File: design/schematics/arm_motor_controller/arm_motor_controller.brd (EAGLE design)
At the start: 71.8 x 54.6 mm, 60 parts, among them Q1 PFET-FQP27P06, Q2 PFET-FQP27P06, Q3 NFET-FQP30N06L, Q4 NFET-FQP30N06L, Q5 PFET-FQP27P06, Q6 PFET-FQP27P06, Q7 NFET-FQP30N06L, Q8 NFET-FQP30N06L, U1 V_REG_LD1085D2

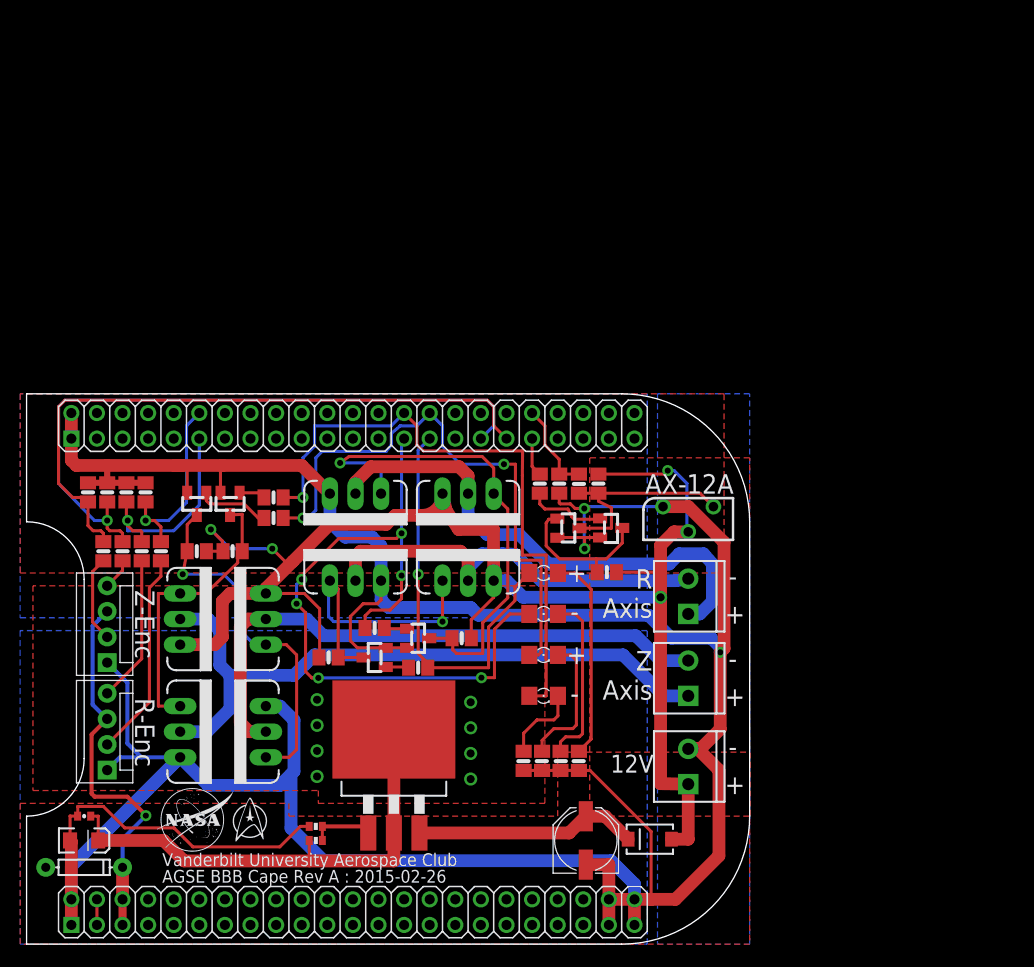
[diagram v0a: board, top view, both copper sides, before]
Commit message: updated adafruit library
to have a version of the board which only shows the outline, but doesn't
set the dimension layer.  also added the adafruit library to the repo
for use with other schematics.
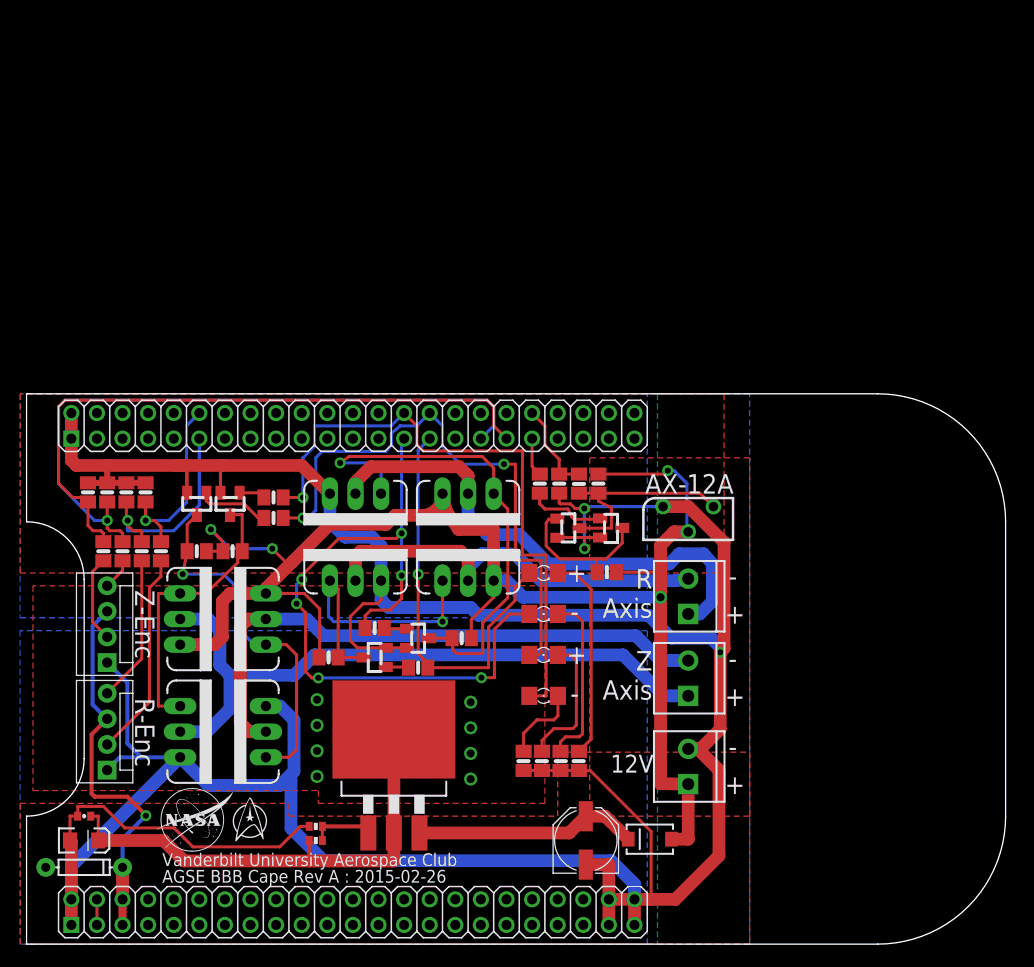
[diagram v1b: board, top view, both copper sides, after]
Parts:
- U$1: value BEAGLEBONE_OUTLINE -> BEAGLEBONE_OUTLINENO_DIM
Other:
- board size 71.8 x 54.6 mm -> 97.2 x 54.6 mm
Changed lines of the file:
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@@
 <layer number="14" name="Route14" color="1" fill="6" visible="no" active="no"/>
 <layer number="15" name="Route15" color="4" fill="6" visible="no" active="no"/>
-<layer number="16" name="Bottom" color="1" fill="1" visible="yes" active="yes"/>
+<layer number="16" name="Bottom" color="1" fill="1" visible="no" active="yes"/>
 <layer number="17" name="Pads" color="2" fill="1" visible="yes" active="yes"/>
 <layer number="18" name="Vias" color="2" fill="1" visible="yes" active="yes"/>
@@
 <layer number="20" name="Dimension" color="15" fill="1" visible="yes" active="yes"/>
 <layer number="21" name="tPlace" color="7" fill="1" visible="yes" active="yes"/>
-<layer number="22" name="bPlace" color="7" fill="1" visible="yes" active="yes"/>
+<layer number="22" name="bPlace" color="7" fill="1" visible="no" active="yes"/>
 <layer number="23" name="tOrigins" color="15" fill="1" visible="yes" active="yes"/>
-<layer number="24" name="bOrigins" color="15" fill="1" visible="yes" active="yes"/>
+<layer number="24" name="bOrigins" color="15" fill="1" visible="no" active="yes"/>
 <layer number="25" name="tNames" color="7" fill="1" visible="yes" active="yes"/>
-<layer number="26" name="bNames" color="7" fill="1" visible="yes" active="yes"/>
+<layer number="26" name="bNames" color="7" fill="1" visible="no" active="yes"/>
 <layer number="27" name="tValues" color="7" fill="1" visible="yes" active="yes"/>
-<layer number="28" name="bValues" color="7" fill="1" visible="yes" active="yes"/>
+<layer number="28" name="bValues" color="7" fill="1" visible="no" active="yes"/>
 <layer number="29" name="tStop" color="7" fill="3" visible="no" active="yes"/>
 <layer number="30" name="bStop" color="7" fill="6" visible="no" active="yes"/>
@@
 <layer number="56" name="wert" color="7" fill="1" visible="no" active="no"/>
 <layer number="57" name="tCAD" color="7" fill="1" visible="no" active="no"/>
+<layer number="59" name="tCarbon" color="7" fill="1" visible="no" active="no"/>
+<layer number="60" name="bCarbon" color="7" fill="1" visible="no" active="no"/>
 <layer number="90" name="Modules" color="5" fill="1" visible="no" active="no"/>
 <layer number="91" name="Nets" color="2" fill="1" visible="no" active="no"/>
@@
 <layer number="113" name="IDFDebug" color="4" fill="1" visible="no" active="yes"/>
 <layer number="116" name="Patch_BOT" color="9" fill="4" visible="no" active="yes"/>
+<layer number="118" name="Rect_Pads" color="7" fill="1" visible="no" active="no"/>
 <layer number="121" name="_tsilk" color="7" fill="1" visible="no" active="yes"/>
 <layer number="122" name="_bsilk" color="7" fill="1" visible="no" active="yes"/>
@@
 <layer number="127" name="_tValues" color="7" fill="1" visible="no" active="yes"/>
 <layer number="128" name="_bValues" color="7" fill="1" visible="no" active="yes"/>
+<layer number="129" name="Mask" color="7" fill="1" visible="no" active="yes"/>
 <layer number="131" name="tAdjust" color="7" fill="1" visible="no" active="yes"/>
 <layer number="132" name="bAdjust" color="7" fill="1" visible="no" active="yes"/>
@@
 <layer number="155" name="FabDoc3" color="7" fill="15" visible="no" active="no"/>
 <layer number="199" name="Contour" color="7" fill="1" visible="no" active="yes"/>
-<layer number="200" name="200bmp" color="1" fill="10" visible="yes" active="yes"/>
+<layer number="200" name="200bmp" color="1" fill="10" visible="no" active="yes"/>
 <layer number="201" name="201bmp" color="2" fill="10" visible="no" active="yes"/>
 <layer number="202" name="202bmp" color="3" fill="1" visible="no" active="no"/>
@@
 <layer number="230" name="230bmp" color="7" fill="1" visible="no" active="yes"/>
 <layer number="231" name="231bmp" color="7" fill="1" visible="no" active="yes"/>
+<layer number="232" name="Eagle3D_PG2" color="7" fill="1" visible="no" active="no"/>
+<layer number="233" name="Eagle3D_PG3" color="7" fill="1" visible="no" active="no"/>
 <layer number="248" name="Housing" color="7" fill="1" visible="no" active="yes"/>
 <layer number="249" name="Edge" color="7" fill="1" visible="no" active="yes"/>
@@
 <rectangle x1="61.7601" y1="38.2905" x2="61.9125" y2="38.3667" layer="22" rot="R180"/>
 <rectangle x1="55.0545" y1="38.2905" x2="55.3593" y2="38.3667" layer="22" rot="R180"/>
+<wire x1="88.519" y1="0.254" x2="4.064" y2="0.254" width="0.127" layer="20"/>
+<wire x1="101.219" y1="42.164" x2="88.519" y2="54.864" width="0.127" layer="20" curve="90"/>
+<wire x1="88.519" y1="0.254" x2="101.219" y2="12.954" width="0.127" layer="20" curve="90"/>
+<wire x1="101.219" y1="42.164" x2="101.219" y2="12.954" width="0.127" layer="20"/>
+<wire x1="88.519" y1="54.864" x2="4.064" y2="54.864" width="0.127" layer="20"/>
+<wire x1="4.064" y1="54.864" x2="4.064" y2="42.164" width="0.127" layer="20"/>
+<wire x1="4.064" y1="12.954" x2="4.064" y2="0.254" width="0.127" layer="20"/>
+<wire x1="9.779" y1="36.449" x2="9.779" y2="18.669" width="0.127" layer="20"/>
+<wire x1="9.779" y1="36.449" x2="4.064" y2="42.164" width="0.127" layer="20" curve="90"/>
+<wire x1="9.779" y1="18.669" x2="4.064" y2="12.954" width="0.127" layer="20" curve="-90"/>
 </plain>
 <attributes>
@@
 </autorouter>
 <elements>
-<element name="U$1" library="adafruit" package="BEAGLEBONE_SHIELD" value="BEAGLEBONE_OUTLINE" x="-10.541" y="54.864" smashed="yes" rot="R270"/>
+<element name="U$1" library="adafruit" package="BEAGLEBONE_SHIELD" value="BEAGLEBONE_OUTLINENO_DIM" x="-10.541" y="54.864" smashed="yes" rot="R270"/>
 <element name="U1" library="SparkFun-PowerIC" package="D2PACK/A" value="V_REG_LD1085D2" x="40.513" y="19.558" smashed="yes">
 <attribute name="MANEX" value="140-0004281" x="40.513" y="19.558" size="1.778" layer="27" display="off"/>
@@
 <signals>
 <signal name="VDD_3V3EXP">
+<wire x1="11.049" y1="4.699" x2="11.049" y2="2.159" width="0.3048" layer="1"/>
 <contactref element="U$1" pad="49"/>
 <contactref element="U$1" pad="50"/>
-<wire x1="11.049" y1="4.699" x2="11.049" y2="2.159" width="0.3048" layer="1"/>
 </signal>
 <signal name="AIN0">

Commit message: working on schematic/board.
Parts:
- removed R1: 370, SparkFun-Passives:0402-RES
- removed R2: 1.5k, SparkFun-Passives:0402-RES
- removed U1: V_REG_LD1085D2, SparkFun-PowerIC:D2PACK/A
- added +HLS, +RLS, -HLS, -RLS: M02POLAR, SparkFun-Connectors:MOLEX-1X2
- added D7: (no value), SparkFun-LED:FKIT-LED-1206
- added LD1085: V_REG_317SINK, SparkFun-PowerIC:TO220-ADJ
- added R28: 50, resistor:M0805
- added SERVO1: AX-12A, molex-spox:SPOX-3
- moved Q7 45.2 mm to (64.5, 20.8), turned to 0 degrees
- moved Q8 37.6 mm to (64.5, 29.3), turned to 180 degrees
- moved Q5 36.0 mm to (53.3, 20.8), turned to 0 degrees
- moved Q3 29.6 mm to (64.4, 34.5), turned to 0 degrees
- moved Q4 28.5 mm to (64.4, 43.2), turned to 180 degrees
- moved R4 26.6 mm to (39.2, 17.1)
- moved R5 26.3 mm to (35.2, 17.1)
- moved Q6 25.7 mm to (53.3, 29.3), turned to 180 degrees
- moved JP1 25.4 mm to (95.1, 16.1)
- moved R-AXIS 25.4 mm to (95.1, 33.0)
- moved SERVO 25.4 mm to (95.1, 42.4)
- moved Z-AXIS 25.4 mm to (95.1, 24.9)
- moved D1 25.3 mm to (91.2, 10.7)
- moved T6 24.8 mm to (80.5, 51.6)
- moved R26 24.4 mm to (83.3, 18.0)
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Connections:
- removed net N$16: R11.2, T4.B
- removed net N$4: R1.1, R2.2, U1.1
- new net +HEIGHT_LS: +HLS.2, R7.2, T2.B, U$1.44
- new net +RADIUS_LS: +RLS.2, R11.2, T4.B, U$1.43
- new net -HEIGHT_LS: -HLS.2, R6.1, T1.B, U$1.42
- new net -RADIUS_LS: -RLS.2, R10.1, T3.B, U$1.41
- new net N$19: U$1.46
- net 12V: now also SERVO1.P$2
- net BBB_TX: now also D7.A
- net GND: now also +HLS.1, +RLS.1, -HLS.1, -RLS.1, LD1085.ADJ, R28.1, SERVO1.P$3; no longer R2.1
- net N$10: now also U$1.45; no longer R7.2, T2.B
- net N$15: now also U$1.14; no longer R10.1, T3.B
- net N$3: now also LD1085.IN; no longer U1.3
- net N$9: now also D7.C, R28.2; no longer R6.1, T1.B
- net SERVO_TX/RX: now also SERVO1.P$1
- net VOUT: now also LD1085.OUT; no longer R1.2, U1.2, U1.TAB
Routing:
- net GND: track 358.6 -> 0.00 mm, vias 3 -> 0
- net 12V: track 151.3 -> 2.03 mm, vias 4 -> 0
- net -RADIUS: track 71.2 -> 0.00 mm, vias 6 -> 0
- net Z+: track 66.6 -> 0.00 mm
- net -HEIGHT: track 61.7 -> 0.00 mm, vias 1 -> 0
- net BBB_EQEP1B: track 66.6 -> 4.87 mm, vias 1 -> 0
- net BBB_EQEP1A: track 63.9 -> 4.87 mm
- net Z-: track 58.9 -> 0.00 mm
- net +HEIGHT: track 56.9 -> 0.00 mm, vias 2 -> 0
- net R+: track 51.0 -> 0.00 mm
- net N$13: track 49.1 -> 0.00 mm, vias 1 -> 0
- net VOUT: track 48.4 -> 0.00 mm, vias 8 -> 0
- net BBB_TX: track 3.84 -> 45.3 mm, vias 0 -> 2
- net R-: track 41.1 -> 0.00 mm
- net +RADIUS: track 40.7 -> 0.00 mm, vias 1 -> 0
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- removed copper zone on layer 16, net 12V
- removed copper zone on layer 1, net GND
- removed copper zone on layer 16, net GND
- removed copper zone on layer 1, net VOUT
- removed copper zone on layer 16, net VOUT

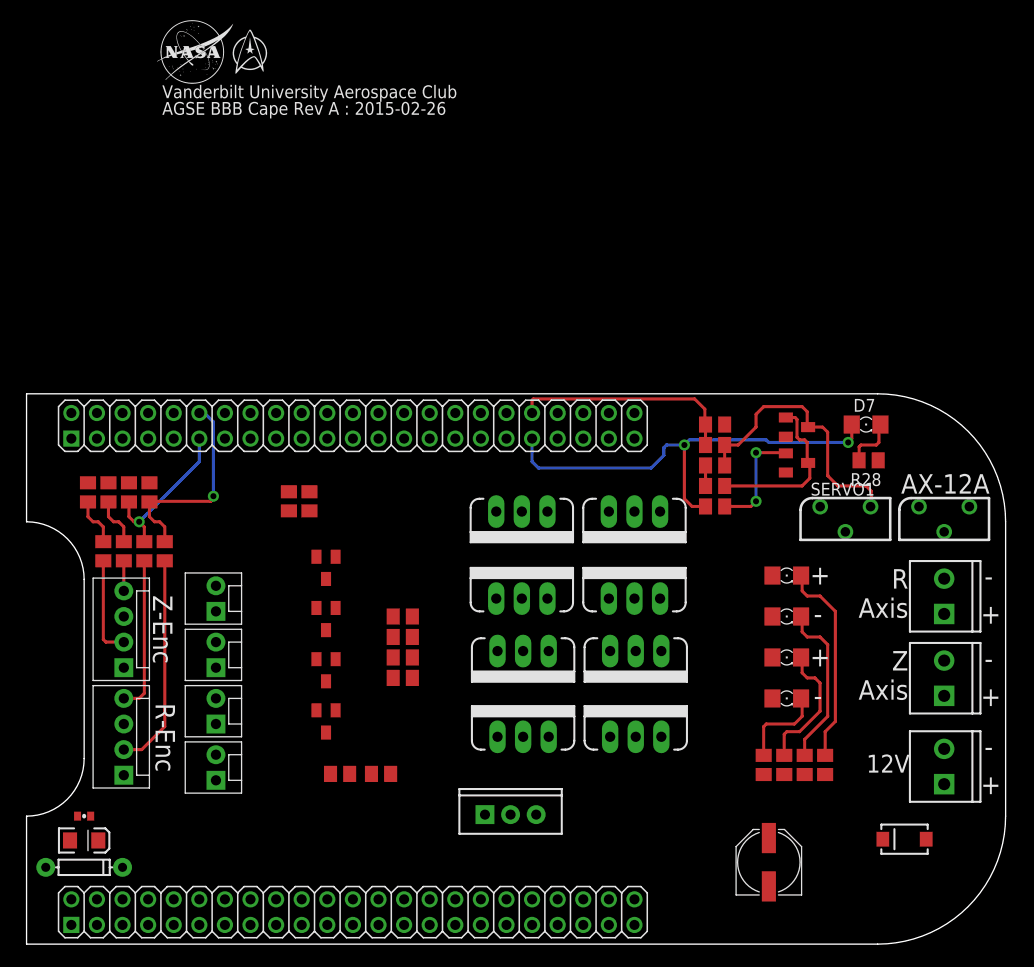
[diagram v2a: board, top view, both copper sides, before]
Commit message: routed the board.
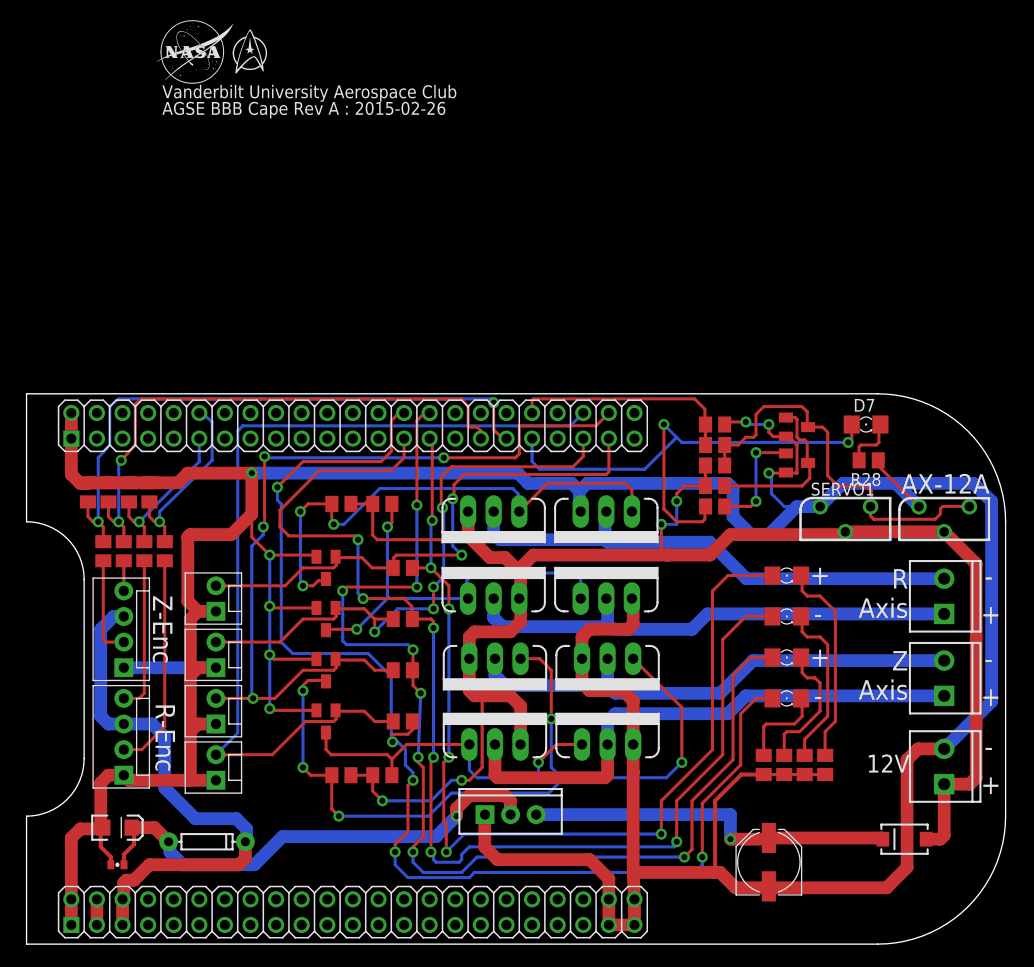
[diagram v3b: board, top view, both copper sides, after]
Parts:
- moved R10 16.3 mm to (41.4, 32.5), turned to 0 degrees
- moved R8 13.4 mm to (39.4, 43.9), turned to 180 degrees
- moved R9 12.7 mm to (35.3, 43.9), turned to 0 degrees
- moved D2 12.5 mm to (22.0, 10.4)
- moved R11 11.4 mm to (41.4, 37.6), turned to 180 degrees
- moved R6 6.35 mm to (41.4, 22.4)
- moved C3 5.85 mm to (13.1, 8.13)
- moved C2 3.54 mm to (13.1, 11.8)
- moved Q5 2.90 mm to (50.5, 20.1)
- moved Q6 2.90 mm to (50.5, 28.6)
- moved Q7 2.90 mm to (61.7, 20.1)
- moved Q8 2.90 mm to (61.7, 28.6)
- moved Q1 2.79 mm to (50.4, 34.5)
- moved Q2 2.79 mm to (50.4, 43.2)
- moved Q3 2.79 mm to (61.6, 34.5)
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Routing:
- net GND: track 0.00 -> 416.1 mm, vias 0 -> 8
- net 12V: track 2.03 -> 166.5 mm, vias 0 -> 4
- net -HEIGHT: track 0.00 -> 121.5 mm, vias 0 -> 5
- net -RADIUS: track 0.00 -> 118.1 mm, vias 0 -> 6
- net +HEIGHT: track 0.00 -> 112.7 mm, vias 0 -> 8
- net +RADIUS: track 0.00 -> 99.0 mm, vias 0 -> 6
- net -HEIGHT_LS: track 0.00 -> 88.5 mm
- net +HEIGHT_LS: track 0.00 -> 82.5 mm, vias 0 -> 4
- net N$8: track 0.00 -> 81.6 mm, vias 0 -> 5
- net -RADIUS_LS: track 0.00 -> 58.4 mm, vias 0 -> 4
- net BBB_EQEP1A: track 4.87 -> 59.7 mm, vias 0 -> 2
- net +RADIUS_LS: track 0.00 -> 54.3 mm, vias 0 -> 2
- net Z+: track 0.00 -> 54.2 mm
- net 5V: track 0.00 -> 53.8 mm
- net N$14: track 0.00 -> 52.3 mm, vias 0 -> 3
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
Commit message: working on updating the board routing.
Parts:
- moved R8 18.3 mm to (39.6, 25.7), turned to 0 degrees
- moved R9 14.9 mm to (39.6, 29.7)
- moved T4 7.77 mm to (32.3, 30.0), turned to 270 degrees
- moved T3 6.78 mm to (32.3, 25.9), turned to 270 degrees
- moved R5 6.29 mm to (39.6, 21.6)
- moved R11 6.11 mm to (39.6, 31.8)
- moved T2 5.79 mm to (32.3, 21.8), turned to 270 degrees
- moved R10 5.14 mm to (39.6, 27.7)
- moved T1 4.82 mm to (32.3, 17.8), turned to 270 degrees
- moved R7 4.20 mm to (39.6, 23.6)
- moved R6 3.31 mm to (39.6, 19.6)
- moved R4 0.57 mm to (39.6, 17.5), turned to 0 degrees
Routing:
- net -RADIUS: track 118.1 -> 32.9 mm, vias 6 -> 4
- net -HEIGHT: track 121.5 -> 43.4 mm, vias 5 -> 2
- net +HEIGHT: track 112.7 -> 39.1 mm, vias 8 -> 2
- net +RADIUS: track 99.0 -> 26.4 mm, vias 6 -> 2
- net GND: track 416.1 -> 372.8 mm, vias 8 -> 3
- net N$13: track 40.7 -> 65.3 mm, vias 2 -> 1
- net N$14: track 52.3 -> 70.4 mm, vias 3 -> 2
- net -HEIGHT_LS: track 88.5 -> 70.7 mm, vias 0 -> 2
- net N$8: track 81.6 -> 67.9 mm, vias 5 -> 2
- net +HEIGHT_LS: track 82.5 -> 69.6 mm, vias 4 -> 2
- net 12V: track 166.5 -> 156.2 mm, vias 4 -> 6
- net N$7: track 34.5 -> 41.9 mm, vias 1 -> 2
- net +RADIUS_LS: track 54.3 -> 57.8 mm, vias 2 -> 0
- net -RADIUS_LS: track 58.4 -> 60.5 mm, vias 4 -> 2
- net R+: track 50.5 -> 49.9 mm
